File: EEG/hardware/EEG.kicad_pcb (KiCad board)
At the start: 2 copper layers, 80 x 80 mm, 107 parts, among them J1 ELECTRODES, J2 2S_BATTERY, J4 POWER_ENABLE, J5 EXTERNAL_ESP32_3V3, J6 USB_C_BENCH_POWER, J7 DEV_POWER_LINK, U1 ADS1299-4, U3 AP63203WU-7, U4 LP2985AIM5-5.0/NOPB, U5 AP3031KTR-G1

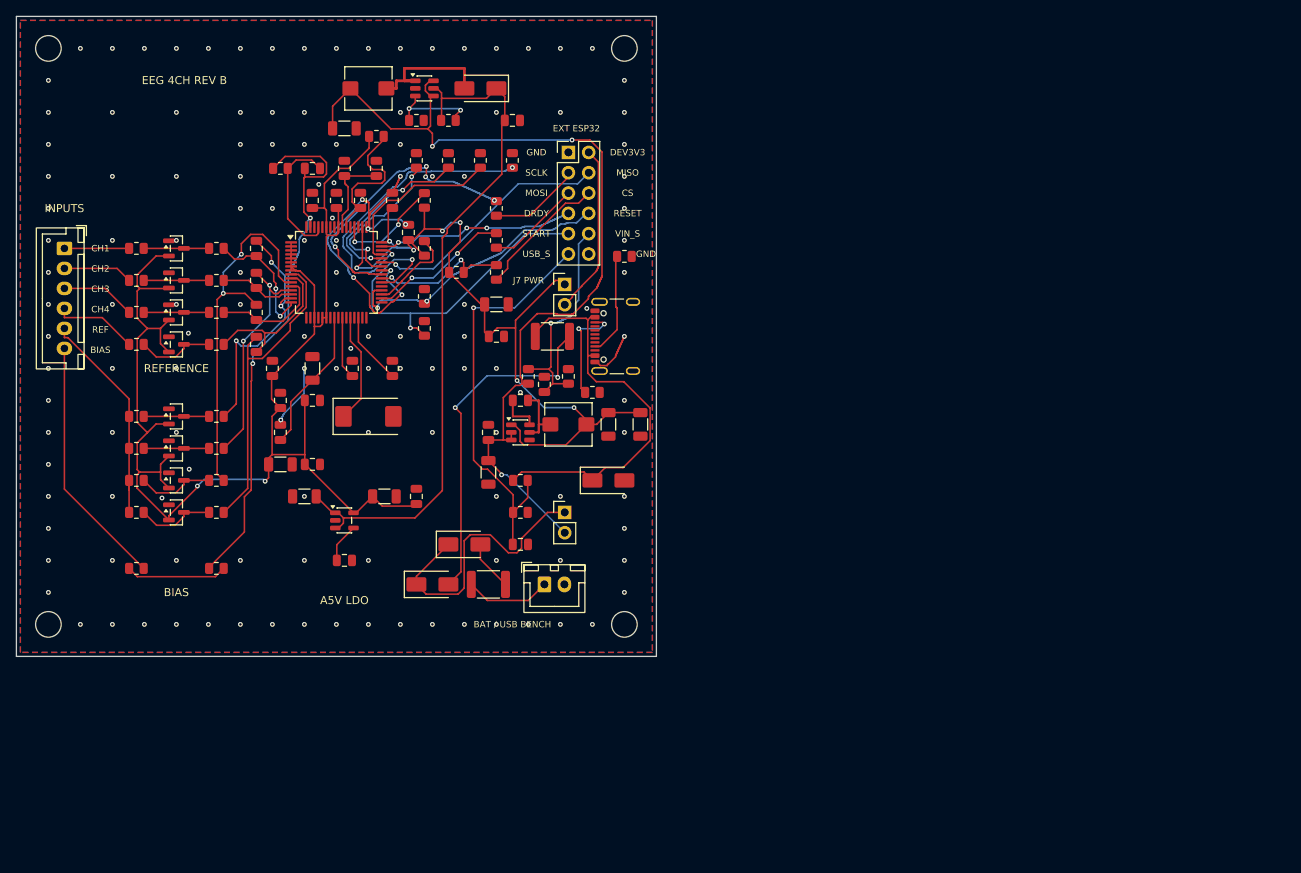
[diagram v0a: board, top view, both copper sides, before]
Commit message: feat(eeg): compact and center PCB, add power LED
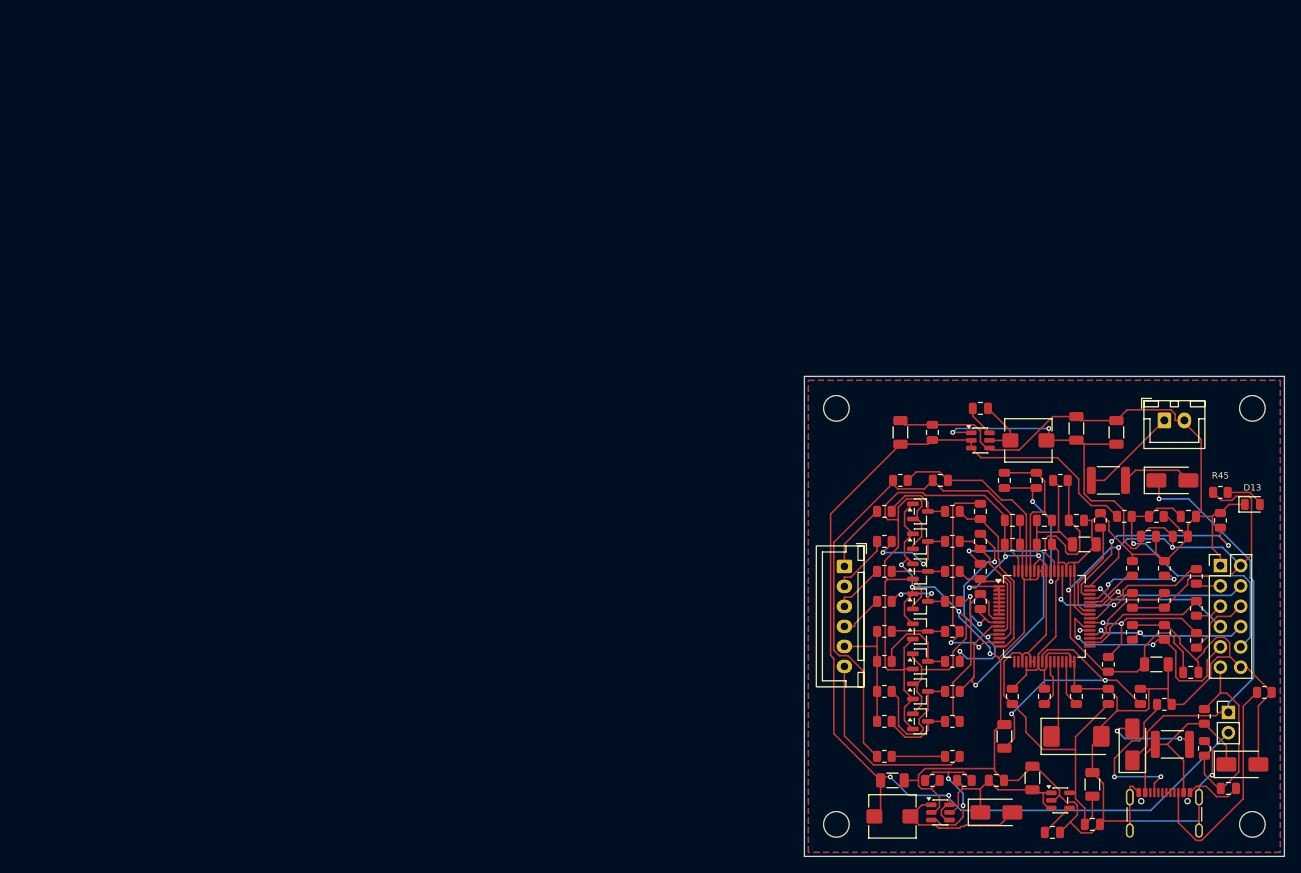
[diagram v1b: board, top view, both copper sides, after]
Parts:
- removed J7: DEV_POWER_LINK, Connector_PinHeader_2.54mm:PinHeader_1x02_P2.54mm_Vertical
- added D13: PWR_GREEN, LED_SMD:LED_0805_2012Metric, F.Cu at (174.5, 91.0)
- added R45: 1k, Resistor_SMD:R_0805_2012Metric, F.Cu at (170.5, 89.5)
- moved C12 112.5 mm to (160.5, 115.0)
- moved L2 112.1 mm to (129.5, 130.0)
- moved D11 111.1 mm to (142.5, 129.5), turned to 0 degrees
- moved U5 111.1 mm to (135.5, 129.5)
- moved C14 109.9 mm to (156.5, 115.0)
- moved MH1 108.3 mm to (122.5, 79.0)
- moved C22 107.1 mm to (165.5, 95.0), turned to 0 degrees
- moved C37 106.5 mm to (129.5, 125.5)
- moved J1 105.3 mm to (123.5, 98.8)
- moved R41 104.7 mm to (138.5, 125.5)
- moved R42 104.7 mm to (134.5, 125.5)
- moved R12 104.7 mm to (137.0, 122.5)
- moved R20 102.4 mm to (163.5, 103.0)
- moved C38 102.3 mm to (142.5, 125.5)
- moved R19 101.6 mm to (159.5, 103.0)
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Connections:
- J5 pad 2: DEV_3V3 -> 3V3
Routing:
- net GND: track 60.9 -> 437.3 mm, vias 142 -> 6
- net BOOST9V: track 86.2 -> 22.8 mm
- net 3V3: track 104.3 -> 144.9 mm, vias 7 -> 5
- net USB_FUSED: track 43.3 -> 11.8 mm
- net USB_PRESENT: track 51.4 -> 25.5 mm, vias 1 -> 0
- net BAT_SW: track 114.7 -> 140.2 mm, vias 3 -> 2
- net USB_VBUS: track 50.2 -> 26.9 mm
- net DEV_3V3: track 21.4 -> 0.00 mm
- net ADC_SCLK: track 36.2 -> 16.3 mm, vias 4 -> 0
- net ADC_START: track 47.8 -> 30.4 mm
- net BAT_PROTECTED: track 36.0 -> 53.2 mm, vias 0 -> 1
- net CH4_N: track 39.6 -> 22.4 mm
- net VREFP: track 18.1 -> 34.6 mm, vias 0 -> 2
- net USB_CC2: track 13.0 -> 29.0 mm, vias 2 -> 0
- net ADC_GPIO2: track 22.3 -> 6.72 mm, vias 2 -> 0
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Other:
- board size 80 x 80 mm -> 60 x 60 mm
- board text removed: "A5V LDO"
- board text removed: "BAT / USB BENCH"
- board text removed: "BIAS"
- board text removed: "CH1"
- board text removed: "CH2"
- board text removed: "CH3"
- board text removed: "CH4"
- board text removed: "CS"
- board text removed: "DEV3V3"
- board text removed: "DRDY"
- board text removed: "EEG 4CH REV B"
- board text removed: "EXT ESP32"
- board text removed: "GND"
- board text removed: "INPUTS"
- board text removed: "J7 PWR"
- board text removed: "MISO"
- board text removed: "MOSI"
- board text removed: "REF"
- board text removed: "REFERENCE"
- board text removed: "RESET"
- board text removed: "SCLK"
- board text removed: "START"
- board text removed: "USB_S"
- board text removed: "VIN_S"
